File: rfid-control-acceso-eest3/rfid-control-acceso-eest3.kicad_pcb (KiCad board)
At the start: 2 copper layers, 140 x 100 mm, 71 parts, among them J1 BOARD_12VDC_2.5A, J10 PIR_TAMPER, J11 PIR_PWR, J12 PIR_ALARM, J13 ESP32-S3-DevKitC-1_N16R8_44P, J2 BUCK?, J5 RC522_8PIN_3V3_XH_CABLE_LECTOR, J6 REED_NC, J8 CABINET_SENSOR, J9 LOCK_12V_1.8A_21.6W, Q1 AO3400A_PRELIM, Q2 AO3400A_PRELIM

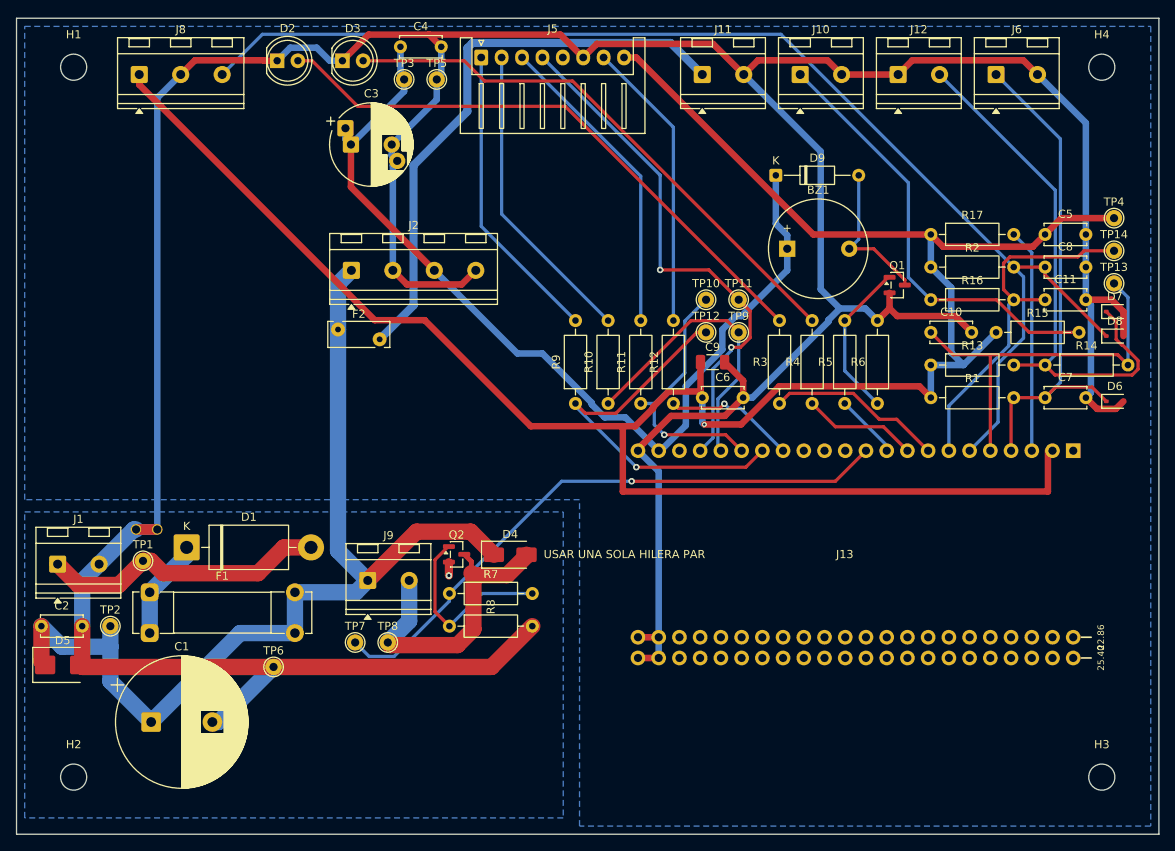
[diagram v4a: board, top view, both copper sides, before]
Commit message: Acerca D4 a J9 y deja el DRC sin infracciones
El emplazamiento dejaba a D4 en (80,50 / 85,75), del lado opuesto de Q2
respecto del conector de carga. Freerouting no tenia como saber que eso esta
mal: para el era un ruteo valido y corto.

Cuando Q2 corta, la bobina de la cerradura no deja de conducir de golpe y su
corriente se va por D4. Todo lo que ese lazo encierra es inductancia parasita,
y esa inductancia aparece como pico de tension sobre el drain del MOSFET. Con
D4 donde estaba, la corriente salia de J9, bajaba hasta TP8, cruzaba al este,
subia y pasaba de largo el MOSFET antes de entrar al diodo.

D4 pasa a (65,58 / 81,95), justo arriba de J9 y con el mismo orden de pines:

  +12V_LOCK (pin 1 -> catodo)   15,78 -> 6,97 mm
  LOCK_OUT  (pin 2 -> anodo)    14,72 -> 6,97 mm

Quedan dos bajadas rectas y paralelas separadas 4,5 mm. La conexion del anodo
al drain va aparte, rodeando el encapsulado por el norte y el este, para no
meter ese recorrido dentro del lazo.

tools/lazo_flyback.py hace el movimiento y el reruteo local; borra las diez
pistas que dejaron de tener sentido y no duplica cobre si se lo corre dos
veces. tools/retoques_finales.py cierra lo que quedaba del DRC:

- J5 pad 6 y J2 pad 4 pasan a conexion solida a plano. El primero tenia un
  solo radio termico y es la masa de retorno del lector RFID; el segundo caia
  en una isla aislada. El alivio termico ahorra calor al soldar y cuesta
  impedancia de retorno, que en un pad de masa de RF es mal negocio.
- Las 28 superposiciones de serigrafia bajan a cero. La reubicacion la dirige
  el DRC de KiCad y no una heuristica propia: un chequeo por caja envolvente
  marca de mas y termina moviendo 66 designadores que estaban bien.

348 pistas, 8 vias, 4 zonas. El DRC pasa sin ninguna infraccion. Los tres no
conectados que quedan son los pines 1 y 2 de J13, deliberados. Sin cambios en
anchos, vias, planos ni en el preruteo bloqueado de la fuente de Q2.

Co-Authored-By: Claude Opus 5 <noreply@anthropic.com>
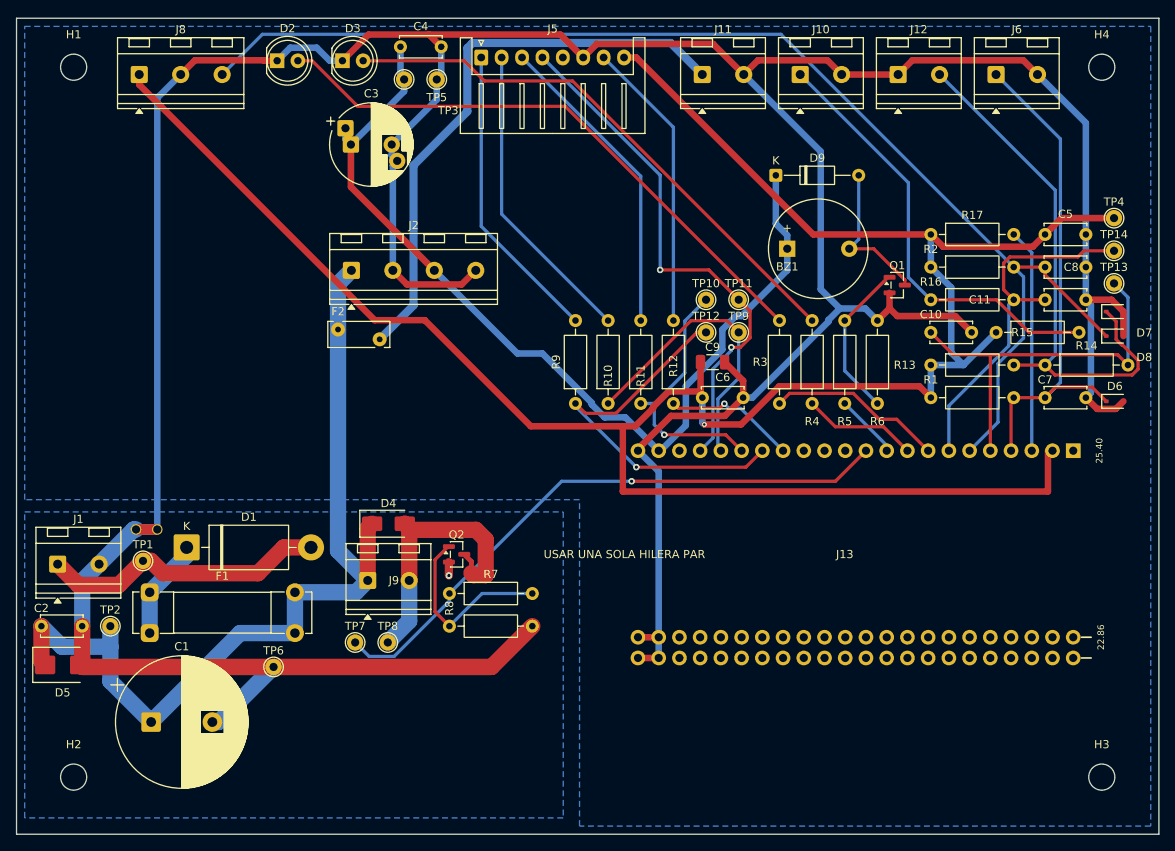
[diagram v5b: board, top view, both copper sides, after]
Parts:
- moved D4 15.4 mm to (65.6, 82.0)
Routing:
- net +12V_LOCK: track 124.2 -> 112.3 mm
- net /6_CERRADURA_12V/LOCK_OUT: track 37.4 -> 35.5 mm
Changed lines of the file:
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@@
 		(tags "Resistor Axial_DIN0207 series Axial Horizontal pin pitch 10.16mm 0.25W = 1/4W length 6.3mm diameter 2.5mm")
 		(property "Reference" "R13"
-			(at 5.08 -2.37 0)
+			(at -3.2 0 0)
 			(layer "F.SilkS")
 			(effects
@@
 			(pinfunction "Pin_6_6")
 			(pintype "passive")
+			(zone_connect 2)
 		)
 		(pad "7" thru_hole oval
@@
 		(tags "ptc resettable fuse polyfuse THT")
 		(property "Reference" "F2"
-			(at 2.55 -1.9 0)
+			(at 0 -2.2 0)
 			(layer "F.SilkS")
 			(effects
@@
 			(pinfunction "Pin_4_4")
 			(pintype "passive")
+			(zone_connect 2)
 		)
 		(embedded_fonts no)
@@
 		(tags "Resistor Axial_DIN0207 series Axial Horizontal pin pitch 10.16mm 0.25W = 1/4W length 6.3mm diameter 2.5mm")
 		(property "Reference" "R8"
-			(at 5.08 -2.37 270)
+			(at 0 -2.2 270)
 			(layer "F.SilkS")
 			(effects
@@
 		(tags "C Disc series Radial pin pitch 5.00mm diameter 5mm width 2.5mm Capacitor")
 		(property "Reference" "C10"
-			(at 2.5 -2.5 0)
+			(at 0 -2.2 0)
 			(layer "F.SilkS")
 			(effects
@@
 		(tags "SOD-323")
 		(property "Reference" "D8"
-			(at 0 -1.85 0)
+			(at 3.6 2.6 0)
 			(layer "F.SilkS")
 			(effects
@@
 		(tags "Resistor Axial_DIN0207 series Axial Horizontal pin pitch 10.16mm 0.25W = 1/4W length 6.3mm diameter 2.5mm")
 		(property "Reference" "R12"
-			(at 5.08 -2.37 270)
+			(at 4.6 0 270)
 			(layer "F.SilkS")
 			(effects
@@
 		(tags "Resistor Axial_DIN0207 series Axial Horizontal pin pitch 10.16mm 0.25W = 1/4W length 6.3mm diameter 2.5mm")
 		(property "Reference" "R6"
-			(at 5.08 -2.37 0)
+			(at -2.2 0 0)
 			(layer "F.SilkS")
 			(effects
@@
 		(tags "test point THT pad")
 		(property "Reference" "TP5"
-			(at 0 -1.998 0)
+			(at 0 2.2 0)
 			(layer "F.SilkS")
 			(effects
@@
 		(tags "Resistor Axial_DIN0207 series Axial Horizontal pin pitch 10.16mm 0.25W = 1/4W length 6.3mm diameter 2.5mm")
 		(property "Reference" "R4"
-			(at 5.08 -2.37 0)
+			(at -2.2 0 0)
 			(layer "F.SilkS")
 			(effects
@@
 		(tags "Resistor Axial_DIN0207 series Axial Horizontal pin pitch 10.16mm 0.25W = 1/4W length 6.3mm diameter 2.5mm")
 		(property "Reference" "R11"
-			(at 5.08 -2.37 270)
+			(at 3.4 0 270)
 			(layer "F.SilkS")
 			(effects
@@
 		(tags "C Disc series Radial pin pitch 5.00mm diameter 5mm width 2.5mm Capacitor")
 		(property "Reference" "C11"
-			(at 2.5 -2.5 0)
+			(at -8 0 0)
 			(layer "F.SilkS")
 			(effects
@@
 		(tags "buzzer")
 		(property "Reference" "BZ1"
-			(at 3.8 -7.2 0)
+			(at 0 2.2 0)
 			(layer "F.SilkS")
 			(effects
@@
 	(footprint "Diode_SMD:D_SMA"
 		(layer "F.Cu")
-		(at 80.5 85.75)
+		(at 65.58 81.95)
 		(descr "Diode SMA (DO-214AC)")
 		(tags "Diode SMA (DO-214AC)")
@@
 		(tags "C Disc series Radial pin pitch 5.00mm diameter 5mm width 2.5mm Capacitor")
 		(property "Reference" "C7"
-			(at 2.5 -2.5 0)
+			(at 0 -2.2 0)
 			(layer "F.SilkS")
 			(effects
@@
 		(tags "Resistor Axial_DIN0207 series Axial Horizontal pin pitch 10.16mm 0.25W = 1/4W length 6.3mm diameter 2.5mm")
 		(property "Reference" "R5"
-			(at 5.08 -2.37 0)
+			(at -2.2 0 0)
 			(layer "F.SilkS")
 			(effects
@@
 		(tags "SOD-323")
 		(property "Reference" "D7"
-			(at 0 -1.85 0)
+			(at 3.6 2.6 0)
 			(layer "F.SilkS")
 			(effects
@@
 		(tags "THT terminal block RND 205-00232 pitch 5.08mm size 10.2x8.45mm drill 1.1mm pad 2.1mm")
 		(property "Reference" "J9"
-			(at 2.54 -5.52 0)
+			(at 3.2 0 0)
 			(layer "F.SilkS")
 			(effects
@@
 		(tags "C Disc series Radial pin pitch 5.00mm diameter 5mm width 2.5mm Capacitor")
 		(property "Reference" "C2"
-			(at 2.5 -2.5 0)
+			(at 0 -2.2 0)
 			(layer "F.SilkS")
 			(effects
@@
 		(tags "Resistor Axial_DIN0207 series Axial Horizontal pin pitch 10.16mm 0.25W = 1/4W length 6.3mm diameter 2.5mm")
 		(property "Reference" "R2"
-			(at 5.08 -2.37 0)
+			(at 0 -2.2 0)
 			(layer "F.SilkS")
 			(effects
@@
 		(tags "Resistor Axial_DIN0207 series Axial Horizontal pin pitch 10.16mm 0.25W = 1/4W length 6.3mm diameter 2.5mm")
 		(property "Reference" "R15"
-			(at 5.08 -2.37 0)
+			(at 3.2 0 0)
 			(layer "F.SilkS")
 			(effects
@@
 		(tags "Resistor Axial_DIN0207 series Axial Horizontal pin pitch 10.16mm 0.25W = 1/4W length 6.3mm diameter 2.5mm")
 		(property "Reference" "R16"
-			(at 5.08 -2.37 0)
+			(at 0 -2.2 0)
 			(layer "F.SilkS")
 			(effects
@@
 		(tags "test point THT pad")
 		(property "Reference" "TP3"
-			(at 0 -1.998 0)
+			(at 5.4 3.8 0)
 			(layer "F.SilkS")
 			(effects
@@
 		(tags "Diode SMB (DO-214AA)")
 		(property "Reference" "D5"
-			(at 0 -3 0)
+			(at 0 3.4 0)
 			(layer "F.SilkS")
 			(effects
@@
 		(tags "C Disc series Radial pin pitch 5.00mm diameter 5mm width 2.5mm Capacitor")
 		(property "Reference" "C8"
-			(at 2.5 -2.5 0)
+			(at 3.2 0 0)
 			(layer "F.SilkS")
 			(effects
@@
 		(tags "Resistor Axial_DIN0207 series Axial Horizontal pin pitch 10.16mm 0.25W = 1/4W length 6.3mm diameter 2.5mm")
 		(property "Reference" "R1"
-			(at 5.08 -2.37 0)
+			(at 0 -2.2 0)
 			(layer "F.SilkS")
 			(effects
@@
 		(tags "Resistor Axial_DIN0207 series Axial Horizontal pin pitch 10.16mm 0.25W = 1/4W length 6.3mm diameter 2.5mm")
 		(property "Reference" "R10"
-			(at 5.08 -2.37 270)
+			(at 3.4 0 270)
 			(layer "F.SilkS")
 			(effects
@@
 			)
 		)
-		(fp_text user "22.86"
-			(at 22.86 -3.4 270)
+		(fp_text user "25.40"
+			(at 0 -3.2 270)
 			(layer "F.SilkS")
 			(effects
@@
 			)
 		)
-		(fp_text user "25.40"
-			(at 25.4 -3.4 270)
+		(fp_text user "22.86"
+			(at 22.86 -3.4 270)
 			(layer "F.SilkS")
 			(effects
@@
 	)
 	(segment
-		(start 75.7489 88.0072)
-		(end 75.9934 88.2517)
+		(start 76.3 82.7)
+		(end 77.5 83.9)
 		(width 2)
 		(layer "F.Cu")
@@
 	)
 	(segment
-		(start 65.8231 96.8231)
-		(end 65.5 96.5)
+		(start 68.12 88.9)
+		(end 68.12 82.49)
 		(width 2)
 		(layer "F.Cu")
@@
 	)
 	(segment
-		(start 75.7489 86.5814)
-		(end 74.8675 85.7)
-		(width 0.601)
+		(start 75.7489 88.0072)
+		(end 75.9934 88.2517)
+		(width 2)
 		(layer "F.Cu")
 		(net "/6_CERRADURA_12V/LOCK_OUT")
 	)
 	(segment
-		(start 75.9934 94.8717)
-		(end 74.042 96.8231)
+		(start 68.12 82.49)
+		(end 67.58 81.95)
 		(width 2)
 		(layer "F.Cu")
@@
 	)
 	(segment
-		(start 75.9934 88.2517)
-		(end 75.9934 94.8717)
-		(width 2)
+		(start 75.7489 86.5814)
+		(end 74.8675 85.7)
+		(width 0.601)
 		(layer "F.Cu")
 		(net "/6_CERRADURA_12V/LOCK_OUT")
 	)
 	(segment
-		(start 75.9934 88.2517)
-		(end 80.1269 88.2517)
+		(start 77.5 83.9)
+		(end 77.5 88.25)
 		(width 2)
 		(layer "F.Cu")
@@
 	)
 	(segment
-		(start 75.7489 88.0072)
-		(end 75.7489 86.5814)
-		(width 0.601)
+		(start 68.33 82.7)
+		(end 76.3 82.7)
+		(width 2)
 		(layer "F.Cu")
 		(net "/6_CERRADURA_12V/LOCK_OUT")
 	)
 	(segment
-		(start 74.042 96.8231)
-		(end 65.8231 96.8231)
+		(start 67.58 81.95)
+		(end 68.33 82.7)
 		(width 2)
 		(layer "F.Cu")
@@
 	)
 	(segment
-		(start 82.5 85.8786)
-		(end 82.5 85.75)
-		(width 2)
+		(start 75.7489 88.0072)
+		(end 75.7489 86.5814)
+		(width 0.601)
 		(layer "F.Cu")
 		(net "/6_CERRADURA_12V/LOCK_OUT")
 	)
 	(segment
-		(start 80.1269 88.2517)
-		(end 82.5 85.8786)
+		(start 77.5 88.25)
+		(end 75.99 88.25)
 		(width 2)
 		(layer "F.Cu")
@@
 	)
 	(segment
-		(start 63.04 88.9)
-		(end 69.02 82.92)
+		(start 63.04 82.49)
+		(end 63.58 81.95)
 		(width 2)
 		(layer "F.Cu")
@@
 	)
 	(segment
-		(start 23.05 98.8)
-		(end 23.05 94.5)
+		(start 63.04 88.9)
+		(end 63.04 82.49)
 		(width 2)
 		(layer "F.Cu")
@@
 	)
 	(segment
-		(start 69.02 82.92)
-		(end 75.67 82.92)
+		(start 23.05 98.8)
+		(end 23.05 94.5)
 		(width 2)
 		(layer "F.Cu")
@@
 		(width 2)
 		(layer "F.Cu")
-		(net "+12V_LOCK")
-	)
-	(segment
-		(start 75.67 82.92)
-		(end 78.5 85.75)
-		(width 2)
-		(layer "F.Cu")
